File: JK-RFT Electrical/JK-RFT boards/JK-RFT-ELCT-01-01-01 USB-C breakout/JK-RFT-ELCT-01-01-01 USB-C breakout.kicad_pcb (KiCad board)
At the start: 2 copper layers, 30 x 25 mm, 5 parts, among them J1 USB_C_Receptacle_USB2.0_16P, J2 Conn_01x04, U1 USBLC6-2SC6

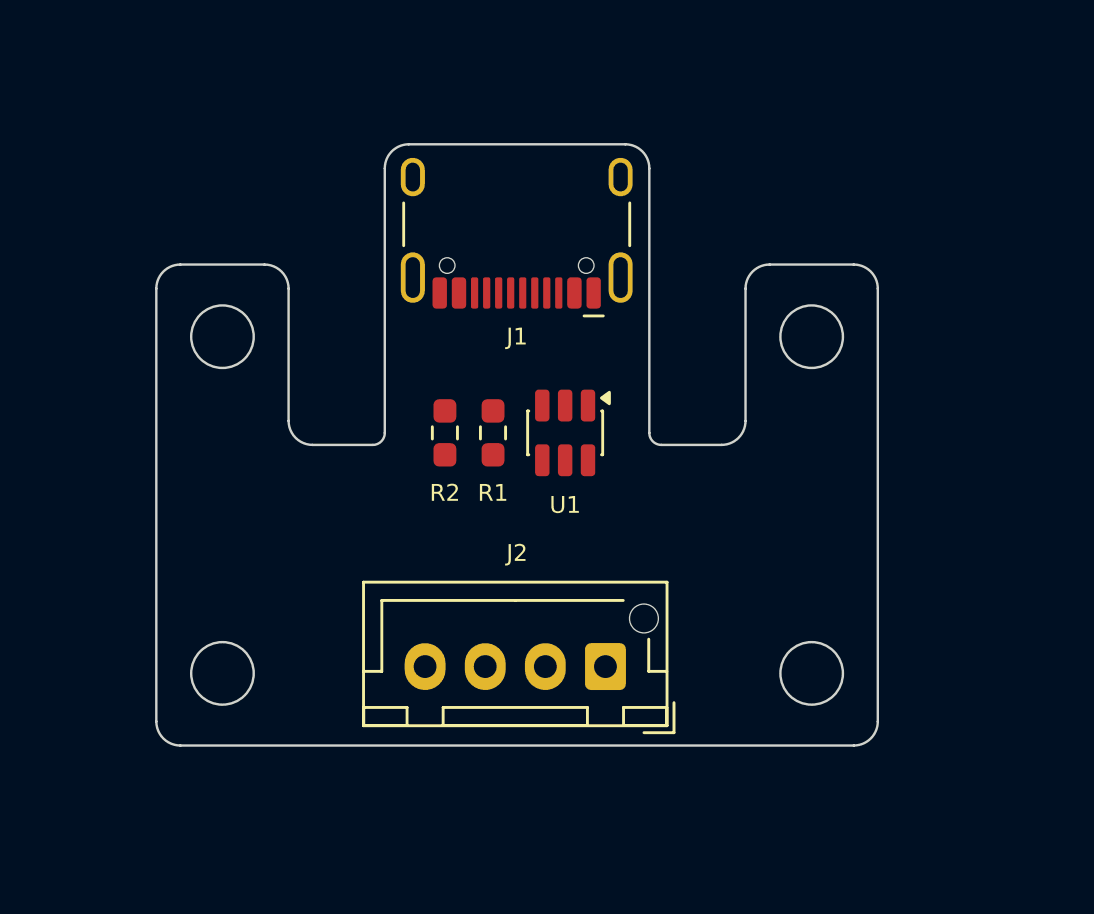
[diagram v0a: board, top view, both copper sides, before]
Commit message: created JK-RFT-ELCT-01-01-01 USB C breakout board
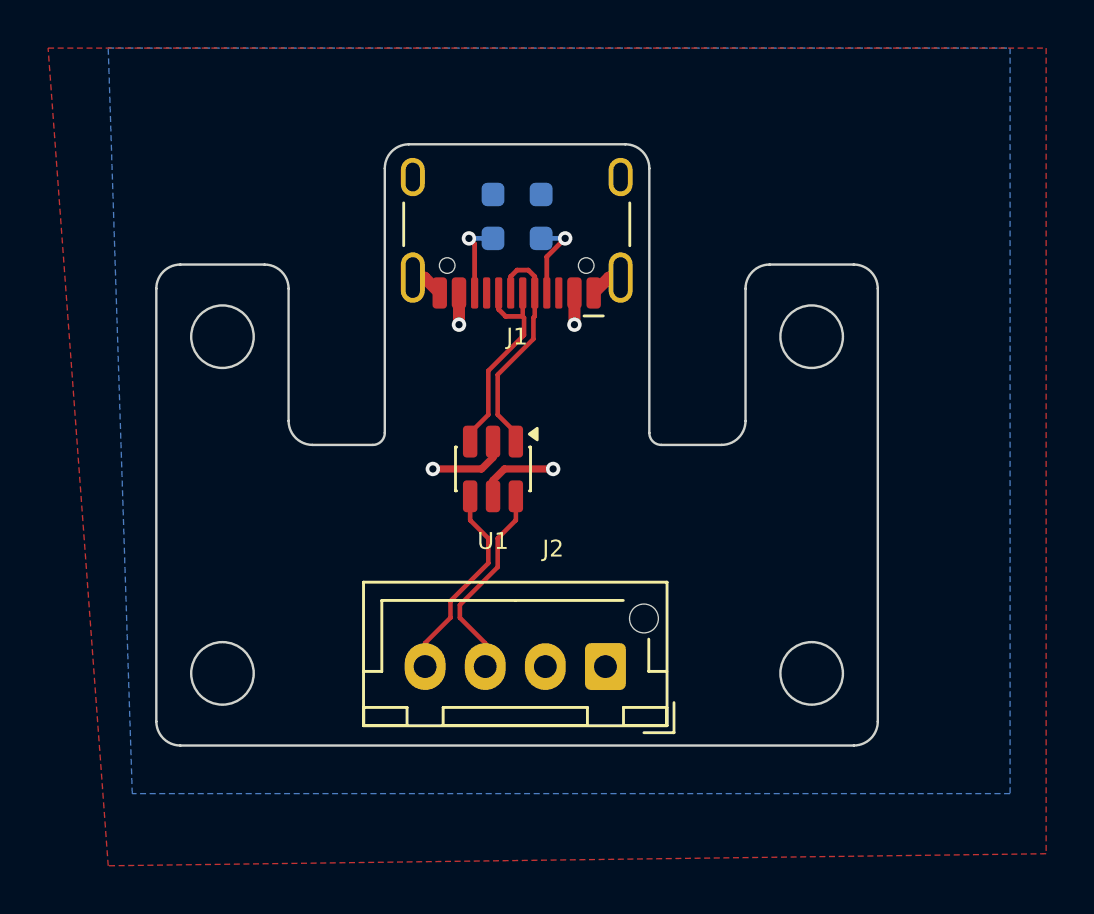
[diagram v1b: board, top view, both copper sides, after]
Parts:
- R1, R2: moved to B.Cu
- moved R1 9.22 mm to (139.5, 92.0), turned to 90 degrees
- moved R2 9.22 mm to (137.5, 92.0), turned to 90 degrees
- moved U1 3.35 mm to (137.5, 102.5)
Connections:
- net Net-(J1-D+-PadA6) renamed /Di+
- net Net-(J1-D--PadA7) renamed /Di-
- net Net-(J2-Pin_3) renamed /Do-
- net Net-(J2-Pin_4) renamed /Do+
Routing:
- net /Di-: track 0.00 -> 9.72 mm
- net /Di+: track 0.00 -> 8.94 mm
- net /Do+: track 0.00 -> 8.48 mm
- net /Do-: track 0.00 -> 8.48 mm
- net GND: track 0.00 -> 6.13 mm, vias 0 -> 1
- net VCC: track 0.00 -> 6.00 mm, vias 0 -> 3
- net Net-(J1-CC1): track 0.00 -> 3.59 mm, vias 0 -> 1
- net Net-(J1-CC2): track 0.00 -> 3.37 mm, vias 0 -> 1
- added copper zone on B.Cu, net GND
- added copper zone on F.Cu, net GND
- added copper zone on In1.Cu, net GND
- added copper zone on In2.Cu, net VCC
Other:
- copper layers 2 -> 4

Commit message: Finalized USB-C breakout board + created USB-C slot in block
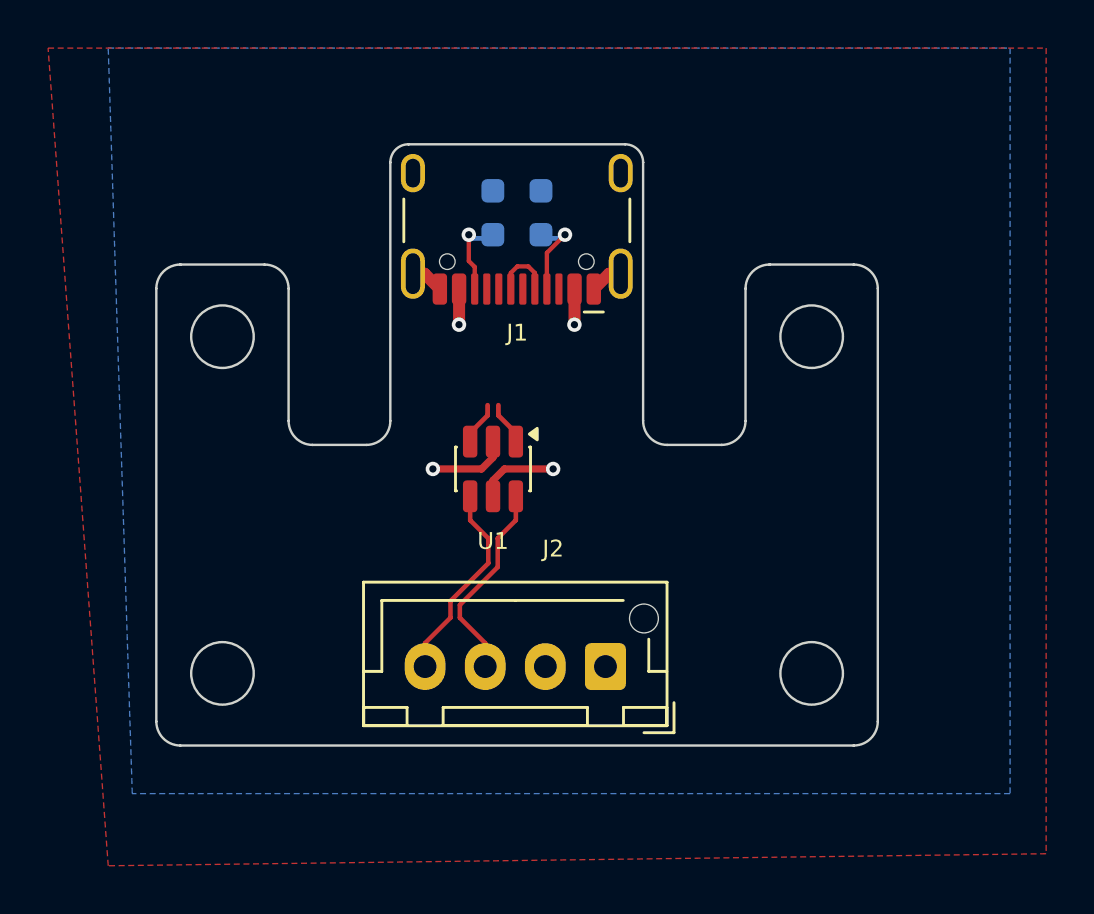
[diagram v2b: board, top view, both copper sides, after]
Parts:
- moved J1 0.16 mm to (138.5, 91.3)
- moved R1 0.15 mm to (139.5, 91.8)
- moved R2 0.15 mm to (137.5, 91.8)
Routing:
- net /Di+: track 8.94 -> 1.81 mm
- net /Di-: track 9.72 -> 4.38 mm
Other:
- outline, holes or cut-outs redrawn
